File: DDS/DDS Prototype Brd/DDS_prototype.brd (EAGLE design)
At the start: 36.3 x 12.7 mm, 27 parts, among them T1 ADTT1-6+, U1 AD9913, U2 S-1711A1818-I6T1U, Y1 TSX-3225 25.0000MF10P-C0

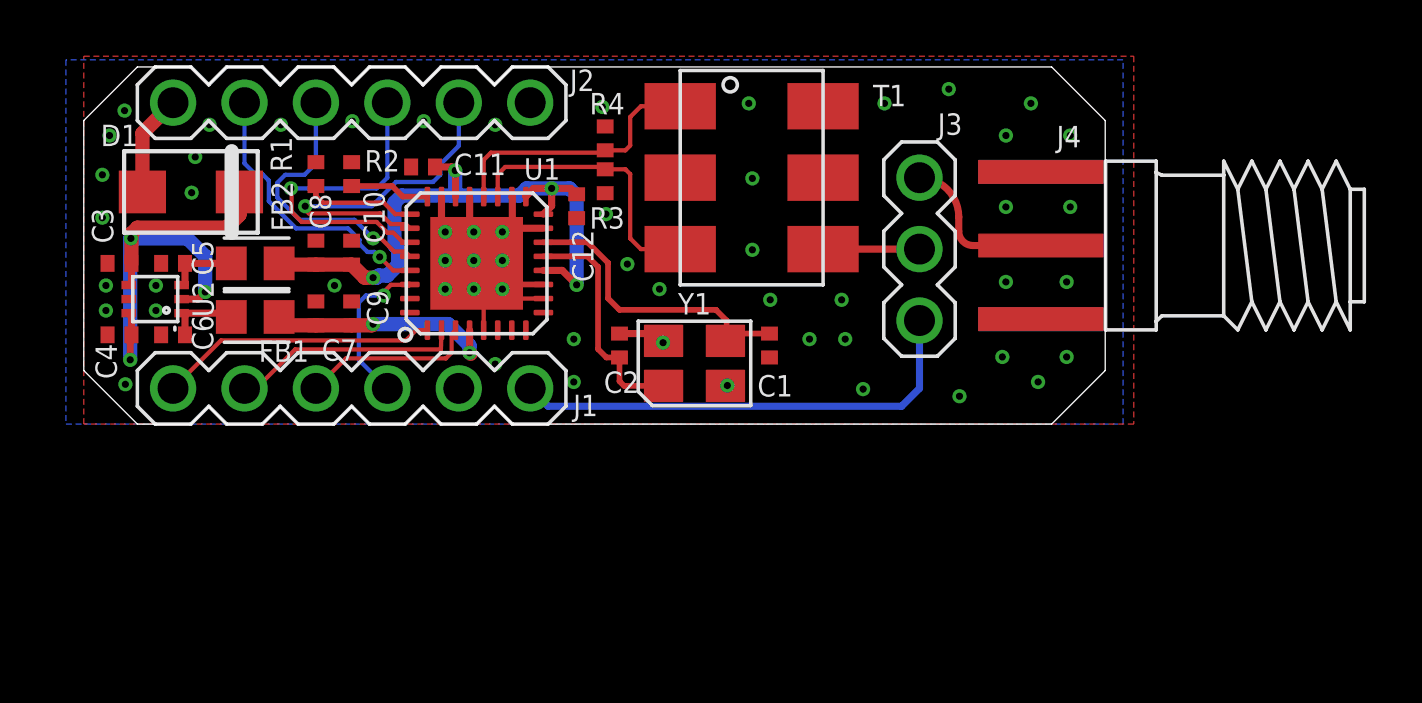
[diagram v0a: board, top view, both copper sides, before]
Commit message: added pull up/down res to ctrl lines
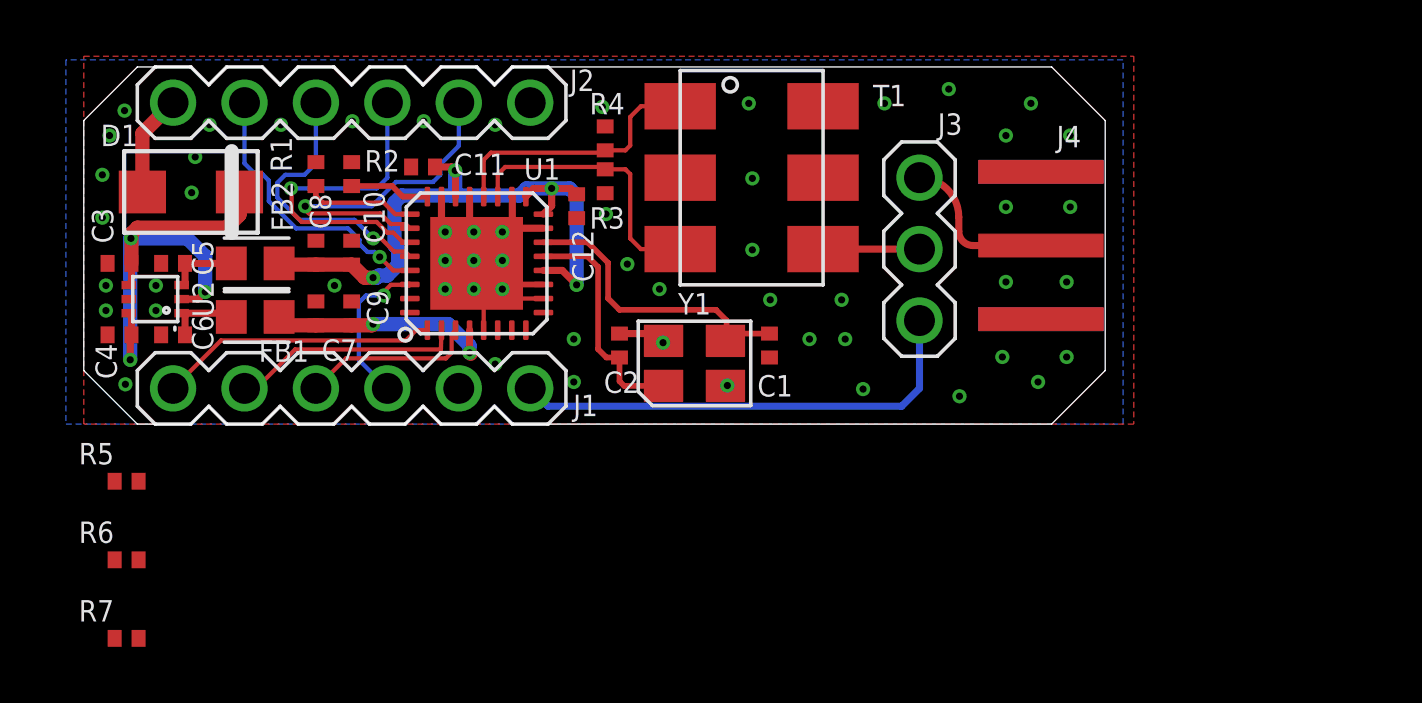
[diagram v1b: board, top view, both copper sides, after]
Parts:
- added R5, R6, R7: 100k, Resistors:0402
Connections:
- net N$1 renamed 3V3_PROT
- net CS_N: now also R5.P$1
- net GND: now also R6.P$1, R7.P$1
- net IO_UPDATE: now also R6.P$2
- net PWR_DWN_CTRL: now also R7.P$2
- net VDD: now also R5.P$2
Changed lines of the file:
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@@
 </layers>
 <board>
+<fusionsync huburn="a.YnVzaW5lc3M6Z21haWwyMTczNDk" projecturn="a.YnVzaW5lc3M6Z21haWwyMTczNDkjRDIwMTkwNjI1MjAwNzYzNTAx" f3durn="urn:adsk.wipprod:dm.lineage:L6iagWy1RZ29c5Tw8XbFRA" pcbguid="8e4313ef-8497-4ae5-8bce-294f77e371e7" lastpulledtime="" lastsyncedchangeguid="c1417b1d-49ee-f0fc-5243-c94c7423e82d"/>
 <plain>
 <wire x1="1.905" y1="0" x2="3.81" y2="0" width="0" layer="20"/>
@@
 <attribute name="NAME" x="9.984" y="8.982" size="0.762" layer="25" font="vector" ratio="15"/>
 </element>
+<element name="R5" library="Resistors" package="0402" value="100k" x="1.524" y="-2.032" smashed="yes">
+<attribute name="NAME" x="-0.176" y="-1.432" size="0.762" layer="25" font="vector" ratio="15"/>
+</element>
+<element name="R6" library="Resistors" package="0402" value="100k" x="1.524" y="-4.826" smashed="yes">
+<attribute name="NAME" x="-0.176" y="-4.226" size="0.762" layer="25" font="vector" ratio="15"/>
+</element>
+<element name="R7" library="Resistors" package="0402" value="100k" x="1.524" y="-7.62" smashed="yes">
+<attribute name="NAME" x="-0.176" y="-7.02" size="0.762" layer="25" font="vector" ratio="15"/>
+</element>
 </elements>
 <signals>
@@
 <wire x1="13.72" y1="3.34" x2="13.72" y2="2.53898125" width="0.254" layer="1"/>
 <wire x1="13.72" y1="2.53898125" x2="13.718509375" y2="2.537490625" width="0.254" layer="1"/>
+<contactref element="R5" pad="P$2"/>
+<wire x1="1.949" y1="-2.032" x2="7.244" y2="3.512" width="0" layer="19" extent="1-1"/>
 </signal>
 <signal name="N$9">
@@
 <via x="0.6604" y="8.8646" extent="1-16" drill="0.254"/>
 <via x="0.6604" y="7.3406" extent="1-16" drill="0.254"/>
+<contactref element="R6" pad="P$1"/>
+<contactref element="R7" pad="P$1"/>
+<wire x1="1.099" y1="-4.826" x2="1.099" y2="-7.62" width="0" layer="19" extent="1-1"/>
+<wire x1="1.479540625" y1="1.41536875" x2="1.099" y2="-4.826" width="0" layer="19" extent="1-1"/>
 </signal>
 <signal name="N$10">
@@
 <wire x1="8.255" y1="9.271" x2="8.255" y2="11.43" width="0.1524" layer="16"/>
 <wire x1="7.8486" y1="8.8646" x2="8.255" y2="9.271" width="0.1524" layer="16"/>
+<contactref element="R5" pad="P$1"/>
+<wire x1="1.099" y1="-2.032" x2="7.6741" y2="7.2644" width="0" layer="19" extent="1-16"/>
 </signal>
 <signal name="IO_UPDATE">
@@
 <wire x1="10.414" y1="8.382" x2="10.795" y2="8.763" width="0.1524" layer="16"/>
 <wire x1="10.795" y1="8.763" x2="10.795" y2="11.43" width="0.1524" layer="16"/>
+<contactref element="R6" pad="P$2"/>
+<wire x1="1.949" y1="-4.826" x2="7.7503" y2="7.1882" width="0" layer="19" extent="1-1"/>
 </signal>
 <signal name="PWR_DWN_CTRL">
@@
 <wire x1="11.1031" y1="8.6106" x2="10.2395" y2="7.747" width="0.1524" layer="16"/>
 <wire x1="12.6774" y1="8.8674" x2="12.4206" y2="8.6106" width="0.1524" layer="16"/>
+<contactref element="R7" pad="P$2"/>
+<wire x1="1.949" y1="-7.62" x2="8.001" y2="7.493" width="0" layer="19" extent="1-1"/>
 </signal>
 <signal name="PS0">
@@
 <wire x1="5.246" y1="3.945" x2="5.246" y2="3.81" width="0.254" layer="1"/>
 </signal>
-<signal name="N$1">
+<signal name="3V3_PROT">
 <contactref element="D1" pad="K"/>
 <contactref element="U2" pad="P2"/>
@@
 </board>
 </drawing>
+<compatibility>
+<note version="8.3" severity="warning">
+Since Version 8.3, EAGLE supports Fusion synchronisation.
+This feature will not be available in this version and saving
+the document will break the link to the Fusion PCB feature.
+</note>
+</compatibility>
 </eagle>

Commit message: routing for pull up and pull down. not done yet.
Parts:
- removed R5: 100k, Resistors:0402
- added D2: (no value), Diodes:0402
- added R8: 470, Resistors:0402
- C9: value 0.1u -> 100p
- moved R7 21.2 mm to (13.5, 9.91)
- moved R6 18.0 mm to (11.9, 9.91), turned to 180 degrees
- moved C12 0.25 mm to (17.8, 7.75)
- moved C11 0.13 mm to (11.9, 9.14)
- flipped J2 to the bottom, turned to 0 degrees
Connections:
- net N$10 renamed RSET
- net N$9 renamed MSTR_RST
- new net N$1: D2.K, R8.P$2
- net 3V3_PROT: now also D2.A
- net CS_N: no longer R5.P$1
- net GND: now also R8.P$1
- net VDD: no longer R5.P$2
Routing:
- net PWR_DWN_CTRL: track 12.2 -> 14.0 mm, vias 1 -> 3
- net 3V3_PROT: track 18.6 -> 19.6 mm
- net N$1: track 0.00 -> 0.85 mm
- net IO_UPDATE: track 11.8 -> 12.6 mm, vias 1 -> 3
- net GND: track 17.6 -> 18.1 mm, vias 56 -> 54
- net SDIO: vias 1 -> 2
- net CS_N: vias 1 -> 2
- net 3V3: vias 0 -> 1

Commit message: final edits to prototype board. added bom.
final edits to prototype board. added bom. made 3d packages.
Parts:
- R1: value (none) -> 100k
- R2: value (none) -> 4.65k
- moved C10 8.34 mm to (17.5, 3.78), turned to 90 degrees
- moved R6 0.74 mm to (11.2, 9.64), flipped to the bottom, turned to 0 degrees
- moved T1 0.61 mm to (23.7, 8.15)
- moved C8 0.59 mm to (8.22, 5.51)
- moved R7 0.34 mm to (13.7, 9.64), flipped to the bottom
- moved R4 0.07 mm to (18.6, 10.2)
- moved R3 0.06 mm to (18.6, 8.64)
- flipped J1 to the bottom, turned to 0 degrees
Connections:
- net PS0: now also J1.P$4; no longer J1.P$3
- net PS1: now also J1.P$3; no longer J1.P$2
- net PS2: now also J1.P$2; no longer J1.P$1
- net SCLK: now also J1.P$1; no longer J1.P$4
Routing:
- net SCLK: track 5.65 -> 10.6 mm, vias 1 -> 0
- net PS0: track 6.21 -> 3.56 mm
- net PS1: track 8.24 -> 5.63 mm, vias 0 -> 1
- net PS2: track 9.90 -> 7.36 mm
- net PWR_DWN_CTRL: track 14.0 -> 12.4 mm, vias 3 -> 1
- net SDIO: track 10.1 -> 11.4 mm, vias 2 -> 1
- net IO_UPDATE: track 12.6 -> 11.8 mm, vias 3 -> 1
- net GND: track 18.1 -> 17.6 mm, vias 54 -> 55
- net CS_N: track 9.92 -> 10.0 mm, vias 2 -> 1
- net 3V3: track 3.63 -> 3.61 mm, vias 1 -> 0

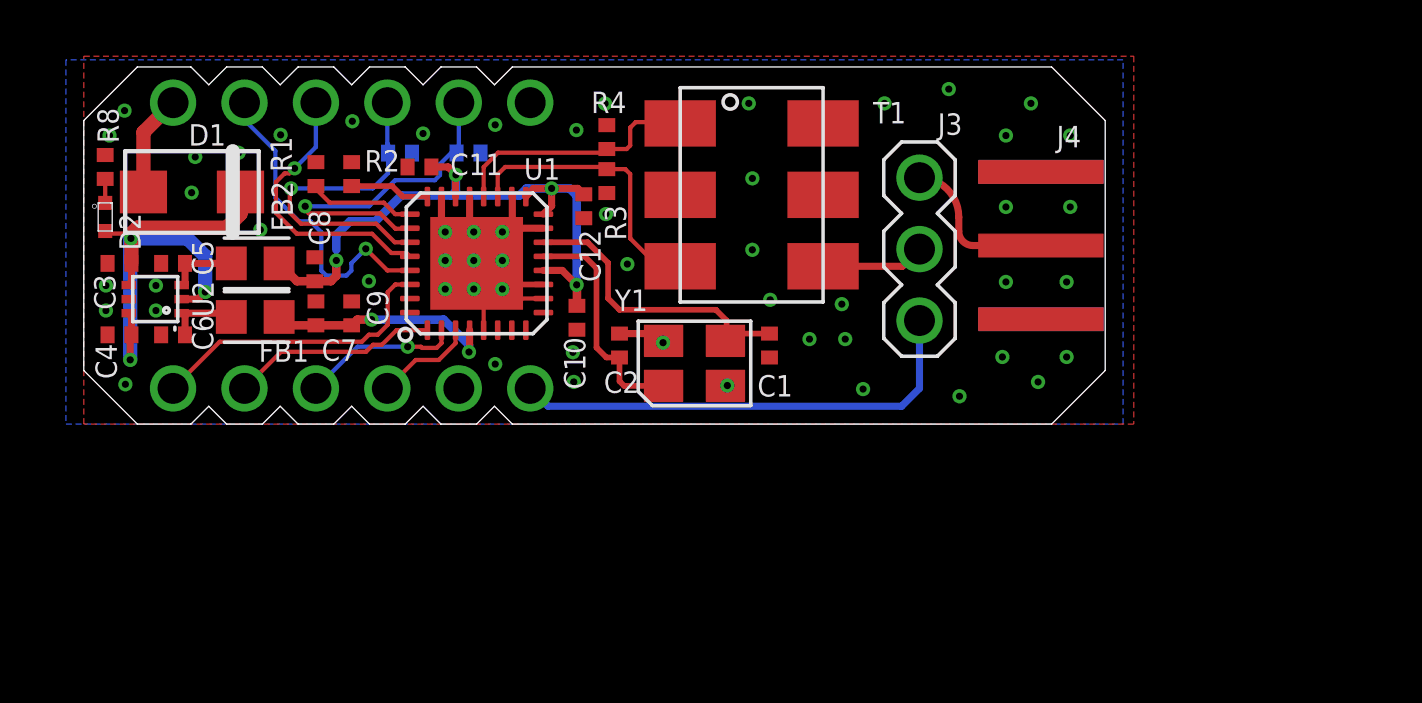
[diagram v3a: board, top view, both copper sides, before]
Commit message: updated board, now has all 3d models, libraried are now managed libs only
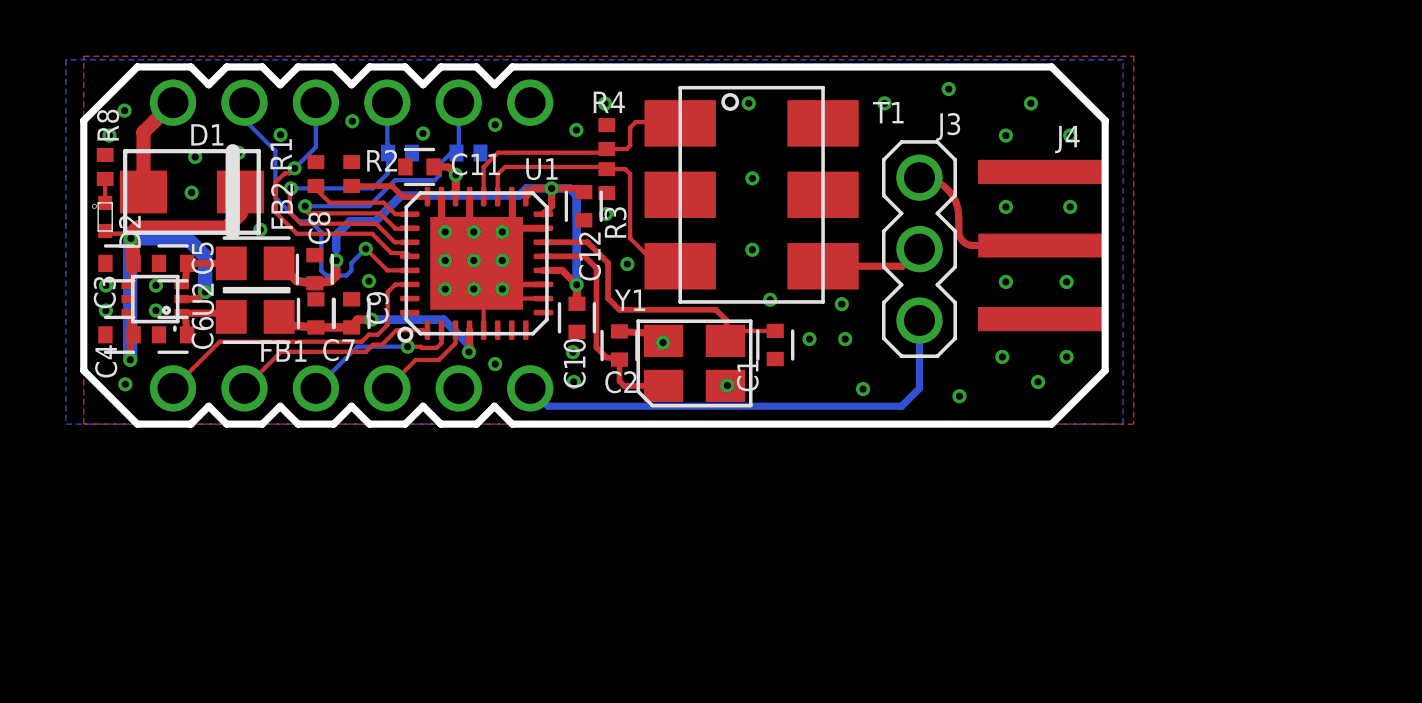
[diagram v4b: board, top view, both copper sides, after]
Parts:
- C10, C4, C5, C6: value 1u -> 1uF
- C11, C3, C7, C8: value 0.1u -> 0.1uF
- C12, C9: value 100p -> 100pF
- D2: device Diodes:0402 -> Diodes:0402_GREEN
- FB1, FB2: value BLM18KG102SN1D -> 1k
- R2: value 4.65k -> 4.64k
- R8: value 470 -> 100
- moved C1 0.21 mm to (24.6, 2.81)
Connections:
- net 3V3_PROT: now also C3.2, C4.2; no longer C3.P$2, C4.P$2
- net GND: now also C1.1, C10.1, C11.1, C12.1, C2.1, C3.1, C4.1, C5.1, C6.1, C7.1, C8.1, C9.1; no longer C1.P$1, C10.P$1, C11.P$1, C12.P$1, C2.P$1, C3.P$1, C4.P$1, C5.P$1, C6.P$1, C7.P$1, C8.P$1, C9.P$1
- net N$14: now also C2.2; no longer C2.P$2
- net N$7: now also C1.2; no longer C1.P$2
- net VCC: now also C10.2, C11.2, C12.2, C8.2; no longer C10.P$2, C11.P$2, C12.P$2, C8.P$2
- net VCC_UNFILT: now also C6.2; no longer C6.P$2
- net VDD: now also C7.2, C9.2; no longer C7.P$2, C9.P$2
- net VDD_UNFILT: now also C5.2; no longer C5.P$2
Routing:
- net N$7: track 10.8 -> 11.3 mm
